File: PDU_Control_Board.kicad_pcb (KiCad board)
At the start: 2 copper layers, 151 parts, among them J1 24V, J10 Precharge_2, J11 Shunt_2, J12 VIN_Enable, J13 VDC_IN_P, J14 VDC_IN_N, J15 VDC_OUT1_P, J16 VDC_OUT1_N, J17 VDC_OUT2_P, J18 VDC_OUT2_N, J19 24V, J2 Shunt_1, J3 SWD, J4 Precharge_1, J5 Precharge_2, J6 Shunt_2, J7 VIN_Enable, J8 Precharge_1, J9 Shunt_1, Q1 BSP75N, Q2 BSP75N, Q3 BSP75N, Q4 BSP75N, Q5 BSP75N, U1 LMV321, U2 APM32F405xG, U3 LMV321, U4 LMV321, U5 LMV321, Y2 X322516MOB4SI

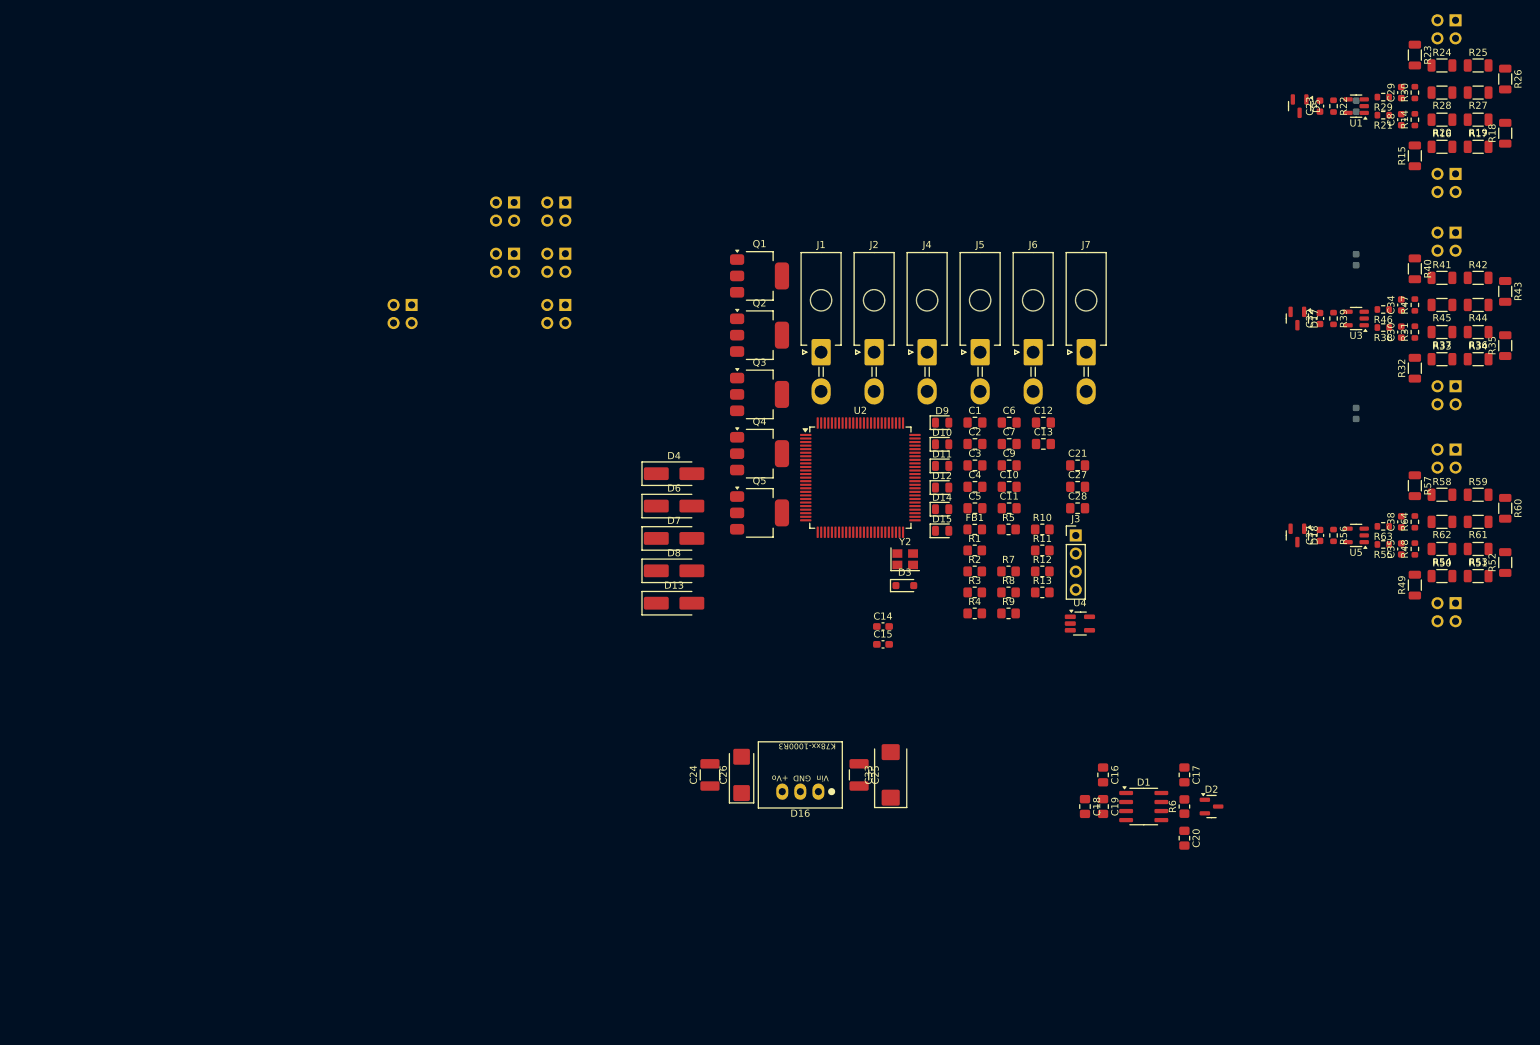
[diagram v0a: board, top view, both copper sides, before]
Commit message: VER1.0: добавил в схему индикацию замыкания
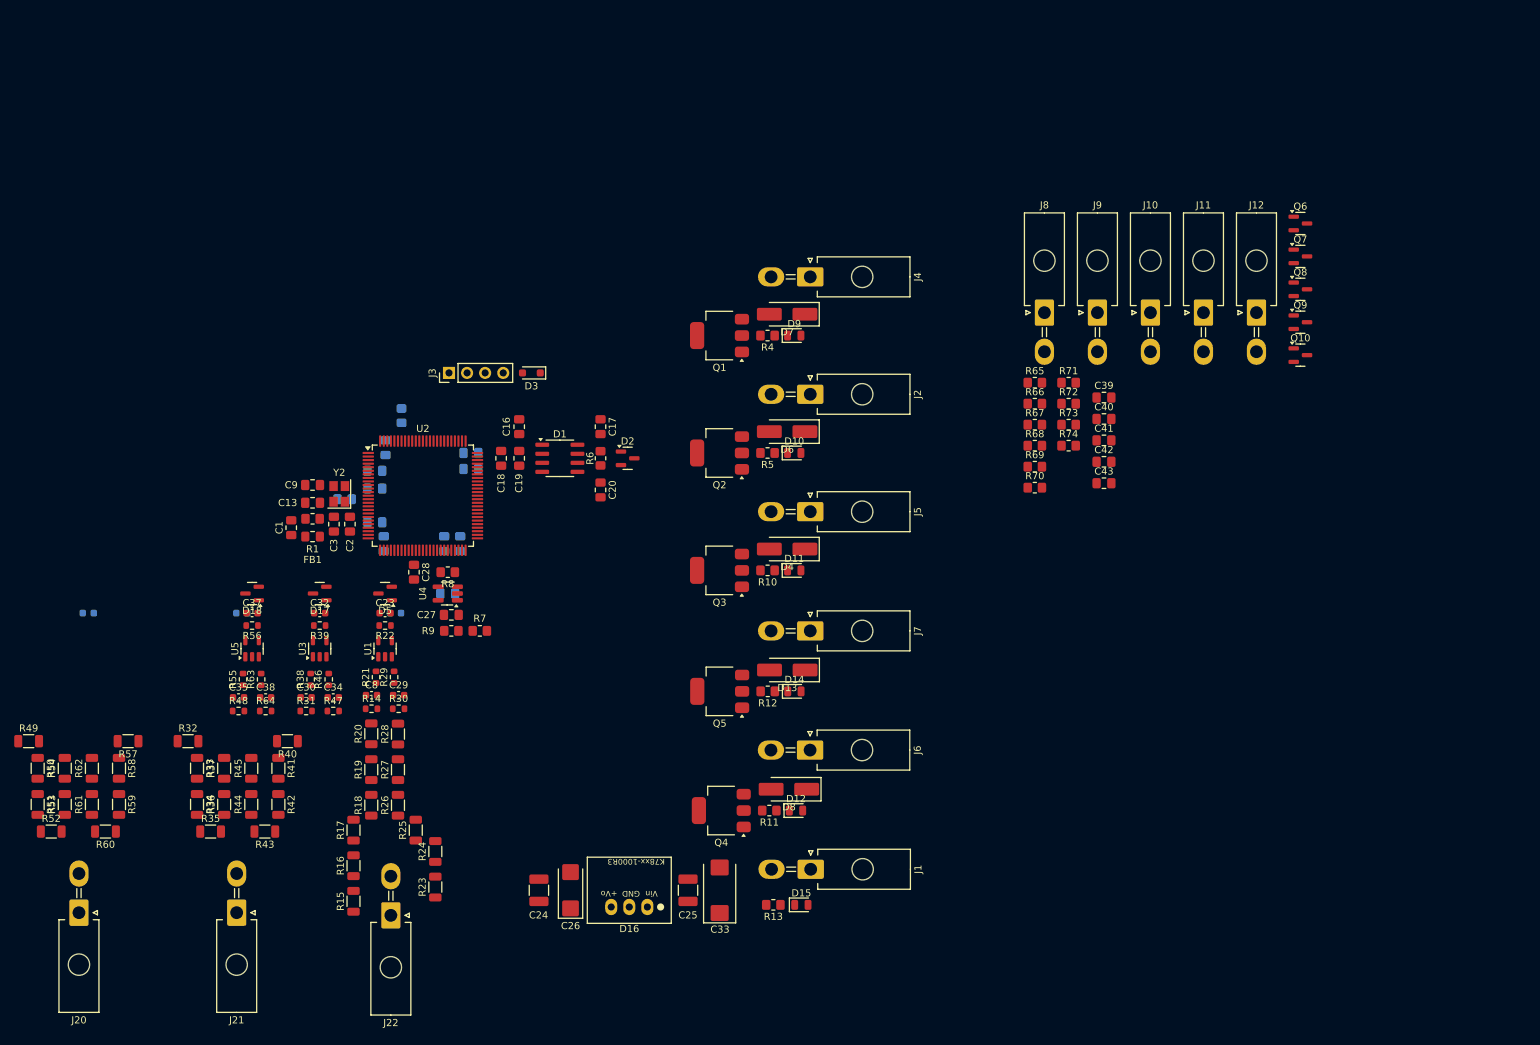
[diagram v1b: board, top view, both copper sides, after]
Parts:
- removed J13: VDC_IN_P, Connector_PinHeader_2.54mm:PinHeader_2x02_P2.54mm_Vertical
- removed J14: VDC_IN_N, Connector_PinHeader_2.54mm:PinHeader_2x02_P2.54mm_Vertical
- removed J15: VDC_OUT1_P, Connector_PinHeader_2.54mm:PinHeader_2x02_P2.54mm_Vertical
- removed J16: VDC_OUT1_N, Connector_PinHeader_2.54mm:PinHeader_2x02_P2.54mm_Vertical
- removed J17: VDC_OUT2_P, Connector_PinHeader_2.54mm:PinHeader_2x02_P2.54mm_Vertical
- removed J18: VDC_OUT2_N, Connector_PinHeader_2.54mm:PinHeader_2x02_P2.54mm_Vertical
- removed J19: 24V, Connector_PinHeader_2.54mm:PinHeader_2x02_P2.54mm_Vertical
- added C39: 2.2u, Capacitor_SMD:C_0805_2012Metric_Pad1.18x1.45mm_HandSolder, F.Cu at (172.2, 89.2)
- added C40: 2.2u, Capacitor_SMD:C_0805_2012Metric_Pad1.18x1.45mm_HandSolder, F.Cu at (172.2, 92.2)
- added C41: 2.2u, Capacitor_SMD:C_0805_2012Metric_Pad1.18x1.45mm_HandSolder, F.Cu at (172.2, 95.2)
- added C42: 2.2u, Capacitor_SMD:C_0805_2012Metric_Pad1.18x1.45mm_HandSolder, F.Cu at (172.2, 98.2)
- added C43: 2.2u, Capacitor_SMD:C_0805_2012Metric_Pad1.18x1.45mm_HandSolder, F.Cu at (172.2, 101.2)
- added J20: VDC_OUT2, Connector_Molex:Molex_Mini-Fit_Jr_5569-02A2_2x01_P4.20mm_Horizontal, F.Cu at (28.2, 161.6)
- added J21: VDC_OUT1, Connector_Molex:Molex_Mini-Fit_Jr_5569-02A2_2x01_P4.20mm_Horizontal, F.Cu at (50.3, 161.6)
- added J22: VDC_IN, Connector_Molex:Molex_Mini-Fit_Jr_5569-02A2_2x01_P4.20mm_Horizontal, F.Cu at (72.0, 162.0)
- added Q10: BC817, Package_TO_SOT_SMD:SOT-23, F.Cu at (199.8, 83.2)
- added Q6: BC817, Package_TO_SOT_SMD:SOT-23, F.Cu at (199.8, 64.8)
- added Q7: BC817, Package_TO_SOT_SMD:SOT-23, F.Cu at (199.8, 69.4)
- added Q8: BC817, Package_TO_SOT_SMD:SOT-23, F.Cu at (199.8, 74.0)
- added Q9: BC817, Package_TO_SOT_SMD:SOT-23, F.Cu at (199.8, 78.6)
- added R65: 2.2k, Resistor_SMD:R_0805_2012Metric_Pad1.20x1.40mm_HandSolder, F.Cu at (162.5, 87.1)
- added R66: 1k, Resistor_SMD:R_0805_2012Metric_Pad1.20x1.40mm_HandSolder, F.Cu at (162.5, 90.1)
- added R67: 2.2k, Resistor_SMD:R_0805_2012Metric_Pad1.20x1.40mm_HandSolder, F.Cu at (162.5, 93.0)
- added R68: 1k, Resistor_SMD:R_0805_2012Metric_Pad1.20x1.40mm_HandSolder, F.Cu at (162.5, 96.0)
- added R69: 2.2k, Resistor_SMD:R_0805_2012Metric_Pad1.20x1.40mm_HandSolder, F.Cu at (162.5, 98.9)
- added R70: 1k, Resistor_SMD:R_0805_2012Metric_Pad1.20x1.40mm_HandSolder, F.Cu at (162.5, 101.9)
- added R71: 2.2k, Resistor_SMD:R_0805_2012Metric_Pad1.20x1.40mm_HandSolder, F.Cu at (167.2, 87.1)
- added R72: 1k, Resistor_SMD:R_0805_2012Metric_Pad1.20x1.40mm_HandSolder, F.Cu at (167.2, 90.1)
- added R73: 2.2k, Resistor_SMD:R_0805_2012Metric_Pad1.20x1.40mm_HandSolder, F.Cu at (167.2, 93.0)
- added R74: 1k, Resistor_SMD:R_0805_2012Metric_Pad1.20x1.40mm_HandSolder, F.Cu at (167.2, 96.0)
- C10, C11, C12, C21, C4, C5, C6, C7, R2, R3: moved to B.Cu
- C14, C15: footprint Capacitor_SMD:C_0603_1608Metric_Pad1.08x0.95mm_HandSolder -> Capacitor_SMD:C_0805_2012Metric_Pad1.18x1.45mm_HandSolder; moved to B.Cu
- J10, J11, J12, J8, J9: footprint Connector_PinHeader_2.54mm:PinHeader_2x02_P2.54mm_Vertical -> Connector_Molex:Molex_Mini-Fit_Jr_5569-02A2_2x01_P4.20mm_Horizontal; moved to F.Cu
- moved R52 207.8 mm to (24.3, 150.2), turned to 0 degrees
- moved R51 204.9 mm to (22.4, 146.4), turned to -90 degrees
- moved R60 201.9 mm to (31.9, 150.2), turned to 180 degrees
- moved R53 201.8 mm to (26.2, 146.4), turned to 90 degrees
- moved R50 199.2 mm to (22.4, 141.3), turned to -90 degrees
- moved R61 198.8 mm to (30.0, 146.4), turned to 90 degrees
- moved R49 196.0 mm to (21.1, 137.5), turned to 0 degrees
- moved R54 196.0 mm to (26.2, 141.3), turned to 90 degrees
- moved R59 195.9 mm to (33.8, 146.4), turned to -90 degrees
- moved R35 194.3 mm to (46.7, 150.2), turned to 0 degrees
- moved R62 192.9 mm to (30.0, 141.3), turned to 90 degrees
- moved C22 191.9 mm to (29.5, 119.5), turned to 0 degrees
- moved R34 190.6 mm to (44.8, 146.4), turned to -90 degrees
- moved R43 190.1 mm to (54.3, 150.2), turned to 180 degrees
- moved R58 189.8 mm to (33.8, 141.3), turned to -90 degrees
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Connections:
- J10 pad 1: unconnected-(J10-Pin_1-Pad1) -> +24V
- J10 pad 2: unconnected-(J10-Pin_2-Pad2) -> Net-(J10-Pin_2)
- J11 pad 1: unconnected-(J11-Pin_1-Pad1) -> +24V
- J11 pad 2: unconnected-(J11-Pin_2-Pad2) -> Net-(J11-Pin_2)
- J12 pad 1: unconnected-(J12-Pin_1-Pad1) -> +24V
- J12 pad 2: unconnected-(J12-Pin_2-Pad2) -> Net-(J12-Pin_2)
- J8 pad 1: unconnected-(J8-Pin_1-Pad1) -> +24V
- J8 pad 2: unconnected-(J8-Pin_2-Pad2) -> Net-(J8-Pin_2)
- J9 pad 1: unconnected-(J9-Pin_1-Pad1) -> +24V
- J9 pad 2: unconnected-(J9-Pin_2-Pad2) -> Net-(J9-Pin_2)
- U2 pad 30: unconnected-(U2-PA5-Pad30) -> VDC_IN_SENSE
- U2 pad 31: unconnected-(U2-PA6-Pad31) -> VDC_OUT1_SENSE
- U2 pad 32: unconnected-(U2-PA7-Pad32) -> VDC_OUT2_SENSE

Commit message: VER1.0: разместил все на плате
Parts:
- added C44: 100n, Capacitor_SMD:C_0805_2012Metric_Pad1.18x1.45mm_HandSolder, B.Cu at (44.0, 115.5)
- added C45: 0.27u, Capacitor_SMD:C_0805_2012Metric_Pad1.18x1.45mm_HandSolder, F.Cu at (44.0, 110.0)
- added C46: 56p, Capacitor_SMD:C_0805_2012Metric_Pad1.18x1.45mm_HandSolder, F.Cu at (44.0, 119.0)
- added D19: LED_Small, LED_SMD:LED_0805_2012Metric, F.Cu at (51.2, 66.5)
- added D20: LED_Small, LED_SMD:LED_0805_2012Metric, F.Cu at (156.9, 40.5)
- added D21: LED_Small, LED_SMD:LED_0805_2012Metric, F.Cu at (157.0, 145.5)
- added D22: LED_Small, LED_SMD:LED_0805_2012Metric, F.Cu at (157.0, 119.3)
- added D23: LED_Small, LED_SMD:LED_0805_2012Metric, F.Cu at (157.0, 92.8)
- added D24: LED_Small, LED_SMD:LED_0805_2012Metric, F.Cu at (157.0, 66.5)
- added D25: LED_Small, LED_SMD:LED_0805_2012Metric, F.Cu at (62.5, 168.5)
- added D26: LED_Small, LED_SMD:LED_0805_2012Metric, F.Cu at (80.8, 168.5)
- added D27: LED_Small, LED_SMD:LED_0805_2012Metric, F.Cu at (99.0, 168.5)
- added D28: BAT54S, Package_TO_SOT_SMD:SOT-23, F.Cu at (44.1, 107.2)
- added J13: 1-776087-1, Connector_My:TE_1-776087-1, F.Cu at (101.5, 52.3)
- added R75: 750, Resistor_SMD:R_0805_2012Metric_Pad1.20x1.40mm_HandSolder, F.Cu at (51.2, 69.0)
- added R76: 5.1k, Resistor_SMD:R_0805_2012Metric_Pad1.20x1.40mm_HandSolder, F.Cu at (153.2, 40.5)
- added R77: 5.1k, Resistor_SMD:R_0805_2012Metric_Pad1.20x1.40mm_HandSolder, F.Cu at (153.2, 145.5)
- added R78: 5.1k, Resistor_SMD:R_0805_2012Metric_Pad1.20x1.40mm_HandSolder, F.Cu at (153.2, 119.3)
- added R79: 5.1k, Resistor_SMD:R_0805_2012Metric_Pad1.20x1.40mm_HandSolder, F.Cu at (153.2, 92.8)
- added R80: 5.1k, Resistor_SMD:R_0805_2012Metric_Pad1.20x1.40mm_HandSolder, F.Cu at (153.2, 66.5)
- added R81: 100k, Resistor_SMD:R_1206_3216Metric_Pad1.30x1.75mm_HandSolder, F.Cu at (53.0, 168.5)
- added R82: 100k, Resistor_SMD:R_1206_3216Metric_Pad1.30x1.75mm_HandSolder, F.Cu at (71.2, 168.5)
- added R83: 100k, Resistor_SMD:R_1206_3216Metric_Pad1.30x1.75mm_HandSolder, F.Cu at (89.5, 168.5)
- added R84: 49.9, Resistor_SMD:R_0805_2012Metric_Pad1.20x1.40mm_HandSolder, F.Cu at (44.0, 112.2)
- added R85: 120, Resistor_SMD:R_0805_2012Metric_Pad1.20x1.40mm_HandSolder, F.Cu at (44.0, 121.2)
- added U6: LMV321, Package_TO_SOT_SMD:SOT-23-5, F.Cu at (44.0, 115.5)
- C22, C23, C29, C30, C31, C32, C34, C35, C36, C37, C38, C8: footprint Capacitor_SMD:C_0603_1608Metric -> Capacitor_SMD:C_0805_2012Metric_Pad1.18x1.45mm_HandSolder
- J1: value 24V -> Current_Sensor; footprint Connector_Molex:Molex_Mini-Fit_Jr_5569-02A2_2x01_P4.20mm_Horizontal -> Connector_Molex:Molex_Mini-Fit_Jr_5569-04A2_2x02_P4.20mm_Horizontal
- R14, R21, R22, R29, R30, R31, R38, R39, R46, R47, R48, R55, R56, R63, R64: footprint Resistor_SMD:R_0603_1608Metric -> Resistor_SMD:R_0805_2012Metric_Pad1.20x1.40mm_HandSolder
- moved D15 135.4 mm to (51.5, 50.0), turned to 180 degrees
- moved R13 135.2 mm to (51.5, 47.5)
- moved C33 135.1 mm to (44.0, 45.5), turned to 180 degrees
- moved C25 129.0 mm to (44.0, 50.0), turned to 0 degrees
- moved D16 117.6 mm to (44.0, 58.2), turned to -90 degrees
- moved C26 106.3 mm to (44.0, 66.5), turned to 180 degrees
- moved C24 100.2 mm to (44.0, 71.0), turned to 180 degrees
- moved Q9 98.5 mm to (132.8, 150.8), turned to 180 degrees
- moved J1 89.0 mm to (42.1, 158.5), turned to 180 degrees
- moved J11 84.1 mm to (145.2, 150.8), turned to -90 degrees
- moved Q8 84.0 mm to (132.8, 124.5), turned to 180 degrees
- moved Q10 76.6 mm to (132.8, 46.3), turned to 180 degrees
- moved D14 75.7 mm to (157.0, 60.3)
- moved R12 75.7 mm to (153.2, 60.3)
- moved Q7 73.0 mm to (132.8, 98.3), turned to 180 degrees
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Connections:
- J1 pad 1: +24V -> unconnected-(J1-Pin_1-Pad1)
- J1 pad 2: GND -> unconnected-(J1-Pin_2-Pad2)
- Q1 pad 1: unconnected-(Q1-G-Pad1) -> Precharge_1
- Q2 pad 1: unconnected-(Q2-G-Pad1) -> Shunt_1
- Q3 pad 1: unconnected-(Q3-G-Pad1) -> Precharge_2
- Q4 pad 1: unconnected-(Q4-G-Pad1) -> Shunt_2
- Q5 pad 1: unconnected-(Q5-G-Pad1) -> VIN_Enable
- R49 pad 2: Net-(R49-Pad2) -> unconnected-(R49-Pad2)
- R50 pad 1: Net-(R49-Pad2) -> unconnected-(R50-Pad1)
- R57 pad 2: Net-(R57-Pad2) -> unconnected-(R57-Pad2)
- R58 pad 1: Net-(R57-Pad2) -> unconnected-(R58-Pad1)
- U2 pad 30: VDC_IN_SENSE -> Current_SENSE
- U2 pad 31: VDC_OUT1_SENSE -> VDC_OUT2_SENSE
- U2 pad 32: VDC_OUT2_SENSE -> VDC_OUT1_SENSE
- U2 pad 33: unconnected-(U2-PC4-Pad33) -> VDC_IN_SENSE
- U2 pad 60: unconnected-(U2-PD13-Pad60) -> Shunt_2
- U2 pad 61: unconnected-(U2-PD14-Pad61) -> ~{Shunt_2_ON}
- U2 pad 62: unconnected-(U2-PD15-Pad62) -> Precharge_2
- U2 pad 63: unconnected-(U2-PC6-Pad63) -> ~{Precharge_2_ON}
- U2 pad 64: unconnected-(U2-PC7-Pad64) -> Shunt_1
- U2 pad 65: unconnected-(U2-PC8-Pad65) -> ~{Shunt_1_ON}
- U2 pad 66: unconnected-(U2-PC9-Pad66) -> Precharge_1
- U2 pad 67: unconnected-(U2-PA8-Pad67) -> ~{Precharge_1_ON}
- U2 pad 68: unconnected-(U2-PA9-Pad68) -> VIN_Enable
- U2 pad 69: unconnected-(U2-PA10-Pad69) -> ~{VIN_Enable_ON}
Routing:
- net Shunt_2: track 0.00 -> 100.4 mm
- net Precharge_2: track 0.00 -> 75.1 mm
- net ~{Shunt_2_ON}: track 0.00 -> 71.7 mm
- net ~{VIN_Enable_ON}: track 0.00 -> 57.3 mm
- net Current_SENSE: track 0.00 -> 56.8 mm
- net Shunt_1: track 0.00 -> 49.6 mm
- net VIN_Enable: track 0.00 -> 46.5 mm
- net ~{Precharge_2_ON}: track 0.00 -> 46.3 mm
- net VDC_OUT2_SENSE: track 0.00 -> 43.6 mm
- net ~{Precharge_1_ON}: track 0.00 -> 32.6 mm
- net Precharge_1: track 0.00 -> 28.9 mm
- net VDC_OUT1_SENSE: track 0.00 -> 25.8 mm
- net ~{Shunt_1_ON}: track 0.00 -> 22.3 mm
- net Net-(J3-Pin_3): track 0.00 -> 19.2 mm
- net CAN1_RXD_MCU: track 0.00 -> 18.0 mm
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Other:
- board outline added: 126.8 x 134.2 mm
- copper layers 2 -> 4

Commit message: VER1.0: добавил на плату все контакторы
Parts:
- added D29: EV200, Contactor_My:EV200, F.Cu at (407.0, 306.1)
- added D30: EV200, Contactor_My:EV200, F.Cu at (407.0, 165.1)
- added D31: EV200, Contactor_My:EV200, F.Cu at (407.0, 235.6)
- added D32: SVC100A, Contactor_My:SVC100A, F.Cu at (357.0, 200.1)
- added D33: SVC100A, Contactor_My:SVC100A, F.Cu at (357.0, 270.6)
- J10, J11, J12, J2, J20, J21, J22, J4, J5, J6, J7, J8, J9: footprint Connector_Molex:Molex_Mini-Fit_Jr_5569-02A2_2x01_P4.20mm_Horizontal -> Connector_My:Mini-Fit_01x02_Vertical
- moved D13 367.0 mm to (374.2, 344.5)
- moved J7 366.5 mm to (377.0, 338.8)
- moved J12 364.0 mm to (377.0, 327.0)
- moved C43 363.8 mm to (357.5, 327.0)
- moved R74 363.8 mm to (359.7, 327.0)
- moved Q10 363.0 mm to (363.0, 327.0)
- moved R73 363.0 mm to (366.2, 327.0)
- moved Q5 358.8 mm to (362.5, 338.8)
- moved D20 350.6 mm to (366.2, 321.8)
- moved R76 350.6 mm to (362.6, 321.7)
- moved D6 348.0 mm to (447.8, 278.8)
- moved J2 347.3 mm to (450.5, 273.0)
- moved D23 346.5 mm to (459.8, 261.2)
- moved R79 346.5 mm to (456.0, 261.2)
- moved C33 346.3 mm to (210.0, 349.5), turned to -90 degrees
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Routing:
- net Shunt_2: track 100.4 -> 19.0 mm
- net Precharge_2: track 75.1 -> 20.2 mm
- net ~{Shunt_2_ON}: track 71.7 -> 19.6 mm
- net Current_SENSE: track 56.8 -> 6.30 mm
- net ~{VIN_Enable_ON}: track 57.3 -> 18.8 mm
- net VDC_OUT2_SENSE: track 43.6 -> 6.34 mm
- net Precharge_1: track 28.9 -> 0.00 mm
- net Shunt_1: track 49.6 -> 21.4 mm
- net VIN_Enable: track 46.5 -> 19.4 mm
- net ~{Precharge_2_ON}: track 46.3 -> 20.8 mm
- net VDC_OUT1_SENSE: track 25.8 -> 6.36 mm
- net ~{Precharge_1_ON}: track 32.6 -> 20.0 mm
- net ~{Shunt_1_ON}: track 22.3 -> 19.6 mm
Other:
- board outline removed
